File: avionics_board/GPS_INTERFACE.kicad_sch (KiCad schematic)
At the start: 2 parts, among them J3 JST socket 6-pin 1mm pitch JS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, J4 Conn_01x05

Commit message: change form factor to 80x80 and cleanup pcb
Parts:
- renumbered J4 to J10, J3 to J11
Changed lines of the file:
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@@
 		(on_board yes)
 		(dnp no)
-		(property "Reference" "J4"
+		(property "Reference" "J10"
 			(at 172.212 101.8032 0)
 			(effects
@@
 			(project ""
 				(path "/f6cc00ab-17f1-4973-862f-7ac95fe70668/00000000-0000-0000-0000-00005ea31c93/00000000-0000-0000-0000-00005eab1057"
-					(reference "J4")
+					(reference "J10")
 					(unit 1)
 				)
@@
 		(on_board yes)
 		(dnp no)
-		(property "Reference" "J3"
+		(property "Reference" "J11"
 			(at 173.355 142.875 0)
 			(effects
@@
 			(project ""
 				(path "/f6cc00ab-17f1-4973-862f-7ac95fe70668/00000000-0000-0000-0000-00005ea31c93/00000000-0000-0000-0000-00005eab1057"
-					(reference "J3")
+					(reference "J11")
 					(unit 1)
 				)

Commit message: avionics board with CAN bus 3.3 to 5V generation
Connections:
- net GND: now also J10.1 (Pin_1); no longer J10.5 (Pin_5)
- net RESET: now also J10.2 (Pin_2); no longer J10.4 (Pin_4)
- net UART_RX: now also J10.5 (Pin_5); no longer J10.1 (Pin_1)
- net UART_TX: now also J10.4 (Pin_4); no longer J10.2 (Pin_2)
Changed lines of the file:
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@@
-	)
-	(symbol
-		(lib_id "Connector_Generic:Conn_01x05")
-		(at 170.18 102.87 0)
-		(unit 1)
-		(exclude_from_sim no)
-		(in_bom yes)
-		(on_board yes)
-		(dnp no)
-		(property "Reference" "J10"
-			(at 172.212 101.8032 0)
-			(effects
-				(font
-					(size 1.27 1.27)
-				)
-				(justify left)
-			)
-		)
-		(property "Value" "Conn_01x05"
-			(at 172.212 104.1146 0)
-			(effects
-				(font
-					(size 1.27 1.27)
-				)
-				(justify left)
-			)
-		)
-		(property "Footprint" "Connector_PinHeader_2.54mm:PinHeader_1x05_P2.54mm_Vertical"
-			(at 170.18 102.87 0)
-			(effects
-				(font
-					(size 1.27 1.27)
-				)
-				(hide yes)
-			)
-		)
-		(property "Datasheet" "~"
-			(at 170.18 102.87 0)
-			(effects
-				(font
-					(size 1.27 1.27)
-				)
-				(hide yes)
-			)
-		)
-		(property "Description" ""
-			(at 170.18 102.87 0)
-			(effects
-				(font
-					(size 1.27 1.27)
-				)
-				(hide yes)
-			)
-		)
-		(property "Mfr. #" "PH1-05-UA"
-			(at 170.18 102.87 0)
-			(effects
-				(font
-					(size 1.27 1.27)
-				)
-				(hide yes)
-			)
-		)
-		(property "Order" "https://www.digikey.com/product-detail/en/adam-tech/PH1-05-UA/2057-PH1-05-UA-ND/9830343"
-			(at 170.18 102.87 0)
-			(effects
-				(font
-					(size 1.27 1.27)
-				)
-				(hide yes)
-			)
-		)
-		(pin "1"
-		)
-		(pin "2"
-		)
-		(pin "3"
-		)
-		(pin "4"
-		)
-		(pin "5"
-		)
-		(instances
-			(project ""
-				(path "/f6cc00ab-17f1-4973-862f-7ac95fe70668/00000000-0000-0000-0000-00005ea31c93/00000000-0000-0000-0000-00005eab1057"
-					(reference "J10")
-					(unit 1)
-				)
-			)
-		)
 	)
 	(symbol
@@
 					(unit 1)
 				)
+			)
+		)
+	)
+	(symbol
+		(lib_id "Connector_Generic:Conn_01x05")
+		(at 170.18 102.87 0)
+		(mirror x)
+		(unit 1)
+		(exclude_from_sim no)
+		(in_bom yes)
+		(on_board yes)
+		(dnp no)
+		(property "Reference" "J10"
+			(at 172.212 103.9368 0)
+			(effects
+				(font
+					(size 1.27 1.27)
+				)
+				(justify left)
+			)
+		)
+		(property "Value" "Conn_01x05"
+			(at 172.212 101.6254 0)
+			(effects
+				(font
+					(size 1.27 1.27)
+				)
+				(justify left)
+			)
+		)
+		(property "Footprint" "Connector_PinHeader_2.54mm:PinHeader_1x05_P2.54mm_Vertical"
+			(at 170.18 102.87 0)
+			(effects
+				(font
+					(size 1.27 1.27)
+				)
+				(hide yes)
+			)
+		)
+		(property "Datasheet" "~"
+			(at 170.18 102.87 0)
+			(effects
+				(font
+					(size 1.27 1.27)
+				)
+				(hide yes)
+			)
+		)
+		(property "Description" ""
+			(at 170.18 102.87 0)
+			(effects
+				(font
+					(size 1.27 1.27)
+				)
+				(hide yes)
+			)
+		)
+		(property "Mfr. #" "PH1-05-UA"
+			(at 170.18 102.87 0)
+			(effects
+				(font
+					(size 1.27 1.27)
+				)
+				(hide yes)
+			)
+		)
+		(property "Order" "https://www.digikey.com/product-detail/en/adam-tech/PH1-05-UA/2057-PH1-05-UA-ND/9830343"
+			(at 170.18 102.87 0)
+			(effects
+				(font
+					(size 1.27 1.27)
+				)
+				(hide yes)
+			)
+		)
+		(pin "1"
+		)
+		(pin "2"
+		)
+		(pin "3"
+		)
+		(pin "4"
+		)
+		(pin "5"
+		)
+		(instances
+			(project "AVIONICS_BOARD"
+				(path "/f6cc00ab-17f1-4973-862f-7ac95fe70668/00000000-0000-0000-0000-00005ea31c93/00000000-0000-0000-0000-00005eab1057"
+					(reference "J10")
+					(unit 1)
+				)

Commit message: cleanup avionics boards after remapping connector
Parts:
- removed J11: JST socket 6-pin 1mm pitch JST SH SM06B-SRSS-TB, Connector_JST:JST_SH_SM06B-SRSS-TB_1x06-1MP_P1.00mm_Horizontal, symbol Connector_Generic:Conn_01x06
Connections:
- no-connect marks 6 -> 5
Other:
- note removed: "GND PWR TXO RXI V_BAT (backup) PWR_CTRL"
- note removed: "GP-735 https://www.sparkfun.com/products/13670"
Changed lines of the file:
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@@
-	)
-	(no_connect
-		(at 165.1 147.32)
 	)
 	(no_connect
@@
 	(wire
 		(pts
-			(xy 157.48 137.16) (xy 165.1 137.16)
-		)
-		(stroke
-			(width 0)
-			(type default)
-		)
-	)
-	(wire
-		(pts
-			(xy 156.21 142.24) (xy 165.1 142.24)
-		)
-		(stroke
-			(width 0)
-			(type default)
-		)
-	)
-	(wire
-		(pts
-			(xy 157.48 139.7) (xy 165.1 139.7)
-		)
-		(stroke
-			(width 0)
-			(type default)
-		)
-	)
-	(wire
-		(pts
-			(xy 157.48 149.86) (xy 165.1 149.86)
-		)
-		(stroke
-			(width 0)
-			(type default)
-		)
-	)
-	(wire
-		(pts
-			(xy 157.48 144.78) (xy 165.1 144.78)
-		)
-		(stroke
-			(width 0)
-			(type default)
-		)
-	)
-	(wire
-		(pts
 			(xy 158.75 97.79) (xy 165.1 97.79)
 		)
@@
 		)
 	)
-	(text "GP-735\nhttps://www.sparkfun.com/products/13670\n\n"
-		(exclude_from_sim no)
-		(at 167.64 133.35 0)
-		(effects
-			(font
-				(size 1.27 1.27)
-			)
-			(justify left bottom)
-		)
-	)
 	(text "For now, just leave open for external modules, no dedicated chip"
 		(exclude_from_sim no)
@@
 		)
 	)
-	(text "GND\nPWR\nTXO\nRXI\nV_BAT (backup)\nPWR_CTRL\n"
-		(exclude_from_sim no)
-		(at 228.6 148.59 0)
-		(effects
-			(font
-				(size 1.27 1.27)
-			)
-			(justify left bottom)
-		)
-	)
-	(hierarchical_label "UART_RX"
-		(shape output)
-		(at 156.21 142.24 180)
-		(fields_autoplaced yes)
-		(effects
-			(font
-				(size 1.27 1.27)
-			)
-			(justify right)
-		)
-	)
 	(hierarchical_label "PWR"
 		(shape input)
@@
 		)
 	)
-	(hierarchical_label "PWR"
-		(shape input)
-		(at 157.48 139.7 180)
-		(fields_autoplaced yes)
-		(effects
-			(font
-				(size 1.27 1.27)
-			)
-			(justify right)
-		)
-	)
 	(hierarchical_label "RESET"
 		(shape input)
@@
 		)
 	)
+	(hierarchical_label "GND"
+		(shape input)
+		(at 97.79 97.79 180)
+		(fields_autoplaced yes)
+		(effects
+			(font
+				(size 1.27 1.27)
+			)
+			(justify right)
+		)
+	)
 	(hierarchical_label "RESET"
 		(shape input)
-		(at 157.48 149.86 180)
-		(fields_autoplaced yes)
-		(effects
-			(font
-				(size 1.27 1.27)
-			)
-			(justify right)
-		)
-	)
-	(hierarchical_label "GND"
-		(shape input)
-		(at 97.79 97.79 180)
-		(fields_autoplaced yes)
-		(effects
-			(font
-				(size 1.27 1.27)
-			)
-			(justify right)
-		)
-	)
-	(hierarchical_label "RESET"
-		(shape input)
 		(at 97.79 105.41 180)
-		(fields_autoplaced yes)
-		(effects
-			(font
-				(size 1.27 1.27)
-			)
-			(justify right)
-		)
-	)
-	(hierarchical_label "GND"
-		(shape input)
-		(at 157.48 137.16 180)
-		(fields_autoplaced yes)
-		(effects
-			(font
-				(size 1.27 1.27)
-			)
-			(justify right)
-		)
-	)
-	(hierarchical_label "UART_TX"
-		(shape input)
-		(at 157.48 144.78 180)
 		(fields_autoplaced yes)
 		(effects
@@
 		)
 	)
-	(symbol
-		(lib_id "Connector_Generic:Conn_01x06")
-		(at 170.18 144.78 0)
-		(mirror x)
-		(unit 1)
-		(exclude_from_sim no)
-		(in_bom yes)
-		(on_board yes)
-		(dnp no)
-		(property "Reference" "J11"
-			(at 173.355 142.875 0)
-			(effects
-				(font
-					(size 1.27 1.27)
-				)
-			)
-		)
-		(property "Value" "JST socket 6-pin 1mm pitch JST SH SM06B-SRSS-TB"
-			(at 198.755 145.415 0)
-			(effects
-				(font
-					(size 1.27 1.27)
-				)
-			)
-		)
-		(property "Footprint" "Connector_JST:JST_SH_SM06B-SRSS-TB_1x06-1MP_P1.00mm_Horizontal"
-			(at 170.18 144.78 0)
-			(effects
-				(font
-					(size 1.27 1.27)
-				)
-				(hide yes)
-			)
-		)
-		(property "Datasheet" "~"
-			(at 170.18 144.78 0)
-			(effects
-				(font
-					(size 1.27 1.27)
-				)
-				(hide yes)
-			)
-		)
-		(property "Description" ""
-			(at 170.18 144.78 0)
-			(effects
-				(font
-					(size 1.27 1.27)
-				)
-				(hide yes)
-			)
-		)
-		(property "Mfr. #" "SM06B-SRSS-TB(LF)(SN)"
-			(at 170.18 144.78 0)
-			(effects
-				(font
-					(size 1.27 1.27)
-				)
-				(hide yes)
-			)
-		)
-		(property "Order" "https://www.digikey.com/product-detail/en/jst-sales-america-inc/SM06B-SRSS-TB-LF-SN/455-1806-1-ND/926877"
-			(at 170.18 144.78 0)
-			(effects
-				(font
-					(size 1.27 1.27)
-				)
-				(hide yes)
-			)
-		)
-		(pin "1"
-		)
-		(pin "2"
-		)
-		(pin "3"
-		)
-		(pin "4"
-		)
-		(pin "5"
-		)
-		(pin "6"
-		)
-		(instances
-			(project ""
-				(path "/f6cc00ab-17f1-4973-862f-7ac95fe70668/00000000-0000-0000-0000-00005ea31c93/00000000-0000-0000-0000-00005eab1057"
-					(reference "J11")
-					(unit 1)
-				)
-			)
-		)
-	)

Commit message: replace nearly all buck converters with boost buck (missing is 5raw
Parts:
- renumbered J10 to J7
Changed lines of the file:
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@@
 		(on_board yes)
 		(dnp no)
-		(property "Reference" "J10"
+		(property "Reference" "J7"
 			(at 172.212 103.9368 0)
 			(effects
@@
 			(project "AVIONICS_BOARD"
 				(path "/f6cc00ab-17f1-4973-862f-7ac95fe70668/00000000-0000-0000-0000-00005ea31c93/00000000-0000-0000-0000-00005eab1057"
-					(reference "J10")
+					(reference "J7")
 					(unit 1)
 				)

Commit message: light sensors with i2c multiplexers for AVI board. i2c amp/volt meter for attitude control coils
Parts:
- renumbered J7 to J6
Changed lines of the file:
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@@
 		(on_board yes)
 		(dnp no)
-		(property "Reference" "J7"
+		(property "Reference" "J6"
 			(at 172.212 103.9368 0)
 			(effects
@@
 			)
 		)
+		(property "Alt" ""
+			(at 170.18 102.87 0)
+			(effects
+				(font
+					(size 1.27 1.27)
+				)
+				(hide yes)
+			)
+		)
 		(pin "1"
 		)
@@
 			(project "AVIONICS_BOARD"
 				(path "/f6cc00ab-17f1-4973-862f-7ac95fe70668/00000000-0000-0000-0000-00005ea31c93/00000000-0000-0000-0000-00005eab1057"
-					(reference "J7")
+					(reference "J6")
 					(unit 1)
 				)

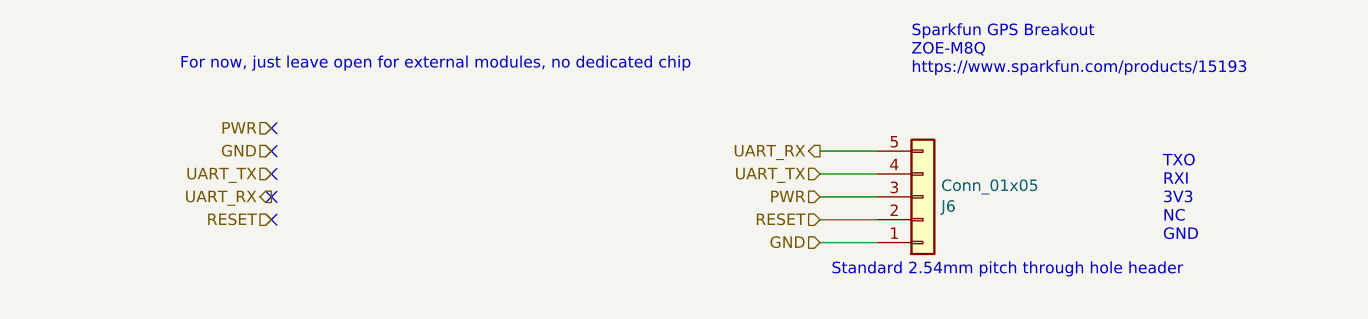
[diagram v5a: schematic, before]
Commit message: assign can power to core powerm will need to use GPIO to enable power stndby from MCUs, finalize pc104 bus assignments
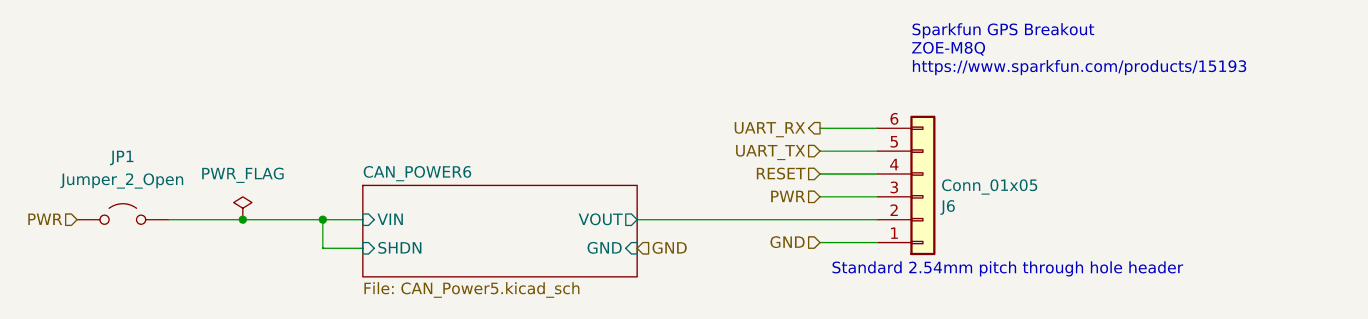
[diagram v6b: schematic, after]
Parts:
- added JP1: Jumper_2_Open, Connector_PinHeader_2.54mm:PinHeader_1x02_P2.54mm_Vertical, symbol Jumper:Jumper_2_Open
- J6: footprint Connector_PinHeader_2.54mm:PinHeader_1x05_P2.54mm_Vertical -> Connector_PinHeader_2.54mm:PinHeader_1x06_P2.54mm_Vertical; symbol Connector_Generic:Conn_01x05 -> Connector_Generic:Conn_01x06
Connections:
- net PWR: now also JP1.1 (A)
- net RESET: now also J6.4 (Pin_4); no longer J6.2 (Pin_2)
- net UART_RX: now also J6.6 (Pin_6); no longer J6.5 (Pin_5)
- net UART_TX: now also J6.5 (Pin_5); no longer J6.4 (Pin_4)
- new net CAN_POWER6/SHDN: JP1.2 (B)
- new net CAN_POWER6/VOUT: J6.2 (Pin_2)
- no-connect marks 5 -> 0
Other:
- added sheet CAN_POWER6 (CAN_Power5.kicad_sch)
- note removed: "For now, just leave open for external modules, no dedicated chip"
- note removed: "TXO RXI 3V3 NC GND"

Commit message: interim checkin before streamlining AVI
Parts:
- J6: Mfr. # PH1-05-UA -> (none)
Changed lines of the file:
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@@
-			)
-		)
-		(property "Mfr. #" "PH1-05-UA"
-			(at 170.18 102.87 0)
-			(effects
-				(font
-					(size 1.27 1.27)
-				)
-				(hide yes)
 			)
 		)
